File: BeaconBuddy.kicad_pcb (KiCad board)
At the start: 2 copper layers, 25.4 x 27.9 mm, 109 parts, among them P1 CONN_01X06, P2 AIN0, U1 nRF52832-QFAA, U2 Si7020-A20, U3 BMP280, Y1 32.768kHz, Y2 32MHz

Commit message: Updated Silk
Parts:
- added REF***: OSHW-Symbol_6.7x6mm_SilkScreen, Symbols:OSHW-Symbol_6.7x6mm_SilkScreen, B.Cu at (172.7, 105.9)
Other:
- board text removed: "Rypple.io"

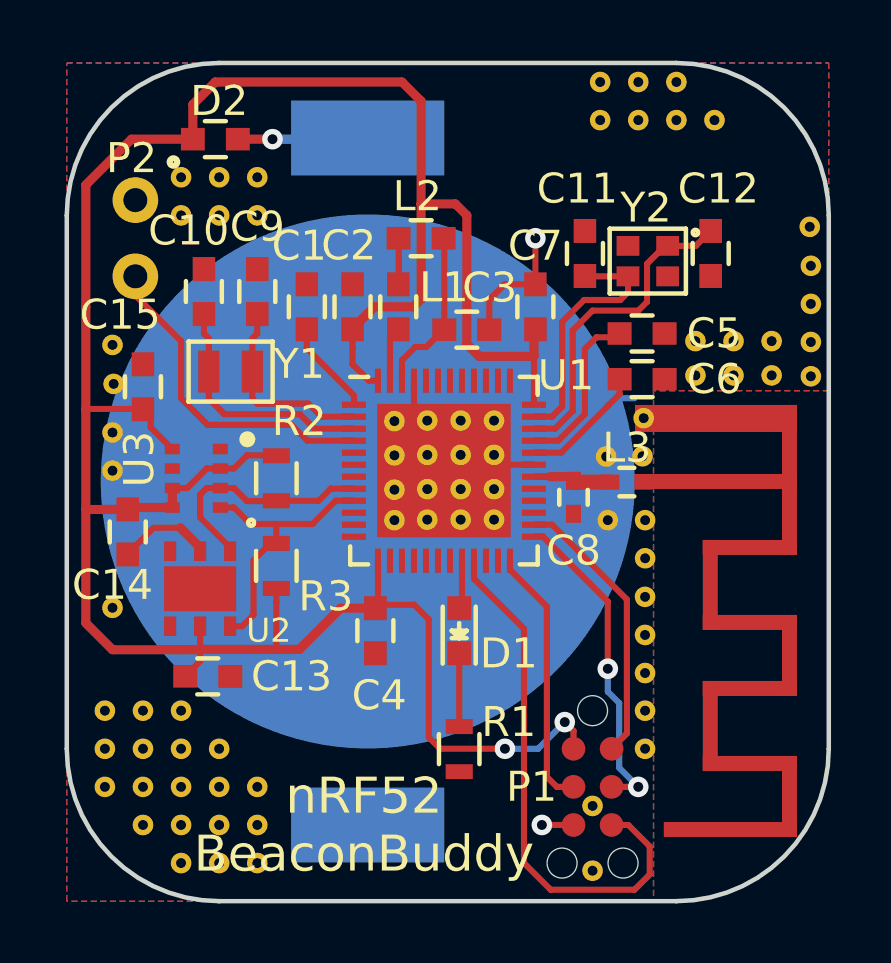
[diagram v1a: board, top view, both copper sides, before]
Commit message: Switch to BME280, update PCB
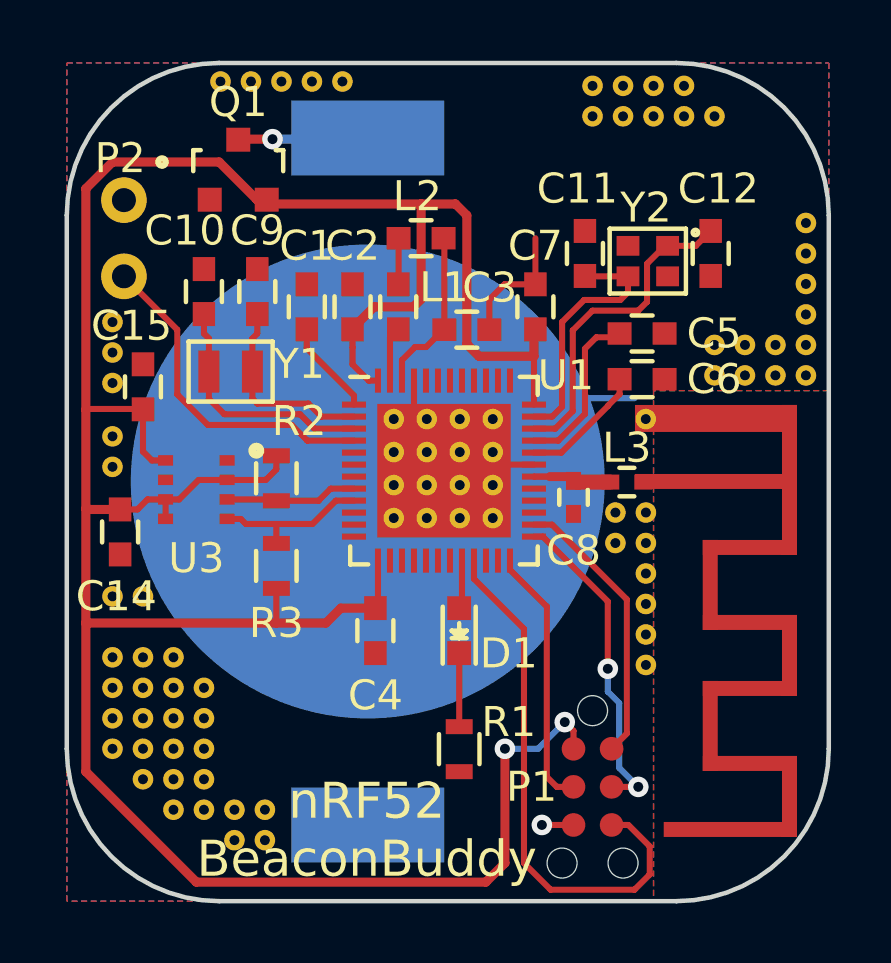
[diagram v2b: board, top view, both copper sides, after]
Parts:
- removed C13: 0.1uF, Capacitors_SMD:C_0603
- removed D2: CDBU0240, Capacitors_SMD:C_0603
- removed the REF** at (171.7, 123.2)
- removed the REF** at (171.6, 112.2)
- removed the REF** at (163.3, 115.6)
- removed the REF** at (164.4, 115.6)
- removed the REF** at (166.6, 115.6)
- removed the REF** at (165.5, 115.6)
- removed the REF** at (163.3, 114.6)
- removed the REF** at (164.4, 114.5)
- removed the REF** at (166.6, 114.5)
- removed the REF** at (165.5, 114.5)
- removed the REF** at (163.3, 113.4)
- removed the REF** at (171.7, 121.9)
- removed the REF** at (164.4, 113.4)
- removed the REF** at (166.6, 113.4)
- removed the REF** at (165.5, 113.4)
- removed the REF** at (166.6, 112.3)
- removed the REF** at (165.5, 112.3)
- removed the REF** at (164.4, 112.3)
- removed the REF** at (163.3, 112.3)
- removed the REF** at (169.9, 127.3)
- removed the REF** at (169.9, 125.1)
- removed the REF** at (153.9, 118.5)
- removed the REF** at (170.4, 115.6)
- removed the REF** at (153.9, 109.7)
- removed the REF** at (153.9, 113.9)
- removed the REF** at (153.9, 112.6)
- removed the REF** at (154.0, 111.0)
- removed the REF** at (171.7, 115.6)
- removed the REF** at (171.7, 116.8)
- removed the REF** at (177.2, 107.1)
- removed the REF** at (177.2, 108.4)
- removed the REF** at (177.2, 109.6)
- removed the REF** at (171.7, 118.1)
- removed the REF** at (177.2, 110.8)
- removed the REF** at (171.7, 119.4)
- removed the REF** at (171.7, 120.7)
- removed the REF** at (175.9, 109.6)
- removed the REF** at (174.6, 109.6)
- removed the REF** at (173.4, 109.6)
- removed the REF** at (177.2, 105.8)
- removed the REF** at (175.9, 110.7)
- removed the REF** at (173.4, 110.7)
- removed the REF** at (174.6, 110.7)
- removed the REF** at (170.4, 113.5)
- removed the REF** at (171.6, 113.4)
- removed REF***: OSHW-Symbol_6.7x6mm_SilkScreen, Symbols:OSHW-Symbol_6.7x6mm_SilkScreen
- removed REF**11, REF**12, REF**21 (x4), REF**22 (x2), REF**31 (x5), REF**32 (x4), REF**41 (x4), REF**42 (x4), REF**51 (x2), REF**52 (x5): Via-13mil, New_Footprints:Via-13mil
- removed U2: Si7020-A20, New_Footprints:S-PWSON-N6
- added Q1: Si2365EDS, TO_SOT_Packages_SMD:SOT-23, F.Cu at (158.1, 103.9)
- added REF**: Via-13mil, new_footprints:Via-13mil, F.Cu at (158.5, 100.9)
- added REF**: Via-13mil, new_footprints:Via-13mil, F.Cu at (166.6, 112.2)
- added REF**: Via-13mil, new_footprints:Via-13mil, F.Cu at (165.5, 112.2)
- added REF**: Via-13mil, new_footprints:Via-13mil, F.Cu at (165.5, 113.3)
- added REF**: Via-13mil, new_footprints:Via-13mil, F.Cu at (166.6, 113.3)
- added REF**: Via-13mil, new_footprints:Via-13mil, F.Cu at (166.6, 114.4)
- added REF**: Via-13mil, new_footprints:Via-13mil, F.Cu at (165.5, 114.4)
- added REF**: Via-13mil, new_footprints:Via-13mil, F.Cu at (165.5, 115.5)
- added REF**: Via-13mil, new_footprints:Via-13mil, F.Cu at (166.6, 115.5)
- added REF**: Via-13mil, new_footprints:Via-13mil, F.Cu at (164.4, 115.5)
- added REF**: Via-13mil, new_footprints:Via-13mil, F.Cu at (164.4, 114.4)
- added REF**: Via-13mil, new_footprints:Via-13mil, F.Cu at (157.5, 100.9)
- added REF**: Via-13mil, new_footprints:Via-13mil, F.Cu at (163.3, 114.4)
- added REF**: Via-13mil, new_footprints:Via-13mil, F.Cu at (163.3, 115.5)
- added REF**: Via-13mil, new_footprints:Via-13mil, F.Cu at (154.9, 118.1)
- added REF**: Via-13mil, new_footprints:Via-13mil, F.Cu at (153.9, 118.1)
- added REF**: Via-13mil, new_footprints:Via-13mil, F.Cu at (153.9, 113.8)
- added REF**: Via-13mil, new_footprints:Via-13mil, F.Cu at (153.9, 112.8)
- added REF**: Via-13mil, new_footprints:Via-13mil, F.Cu at (153.9, 109.0)
- added REF**: Via-13mil, new_footprints:Via-13mil, F.Cu at (153.9, 110.0)
- added REF**: Via-13mil, new_footprints:Via-13mil, F.Cu at (153.9, 111.0)
- added REF**: Via-13mil, new_footprints:Via-13mil, F.Cu at (159.0, 126.2)
- added REF**: Via-13mil, new_footprints:Via-13mil, F.Cu at (161.6, 100.9)
- added REF**: Via-13mil, new_footprints:Via-13mil, F.Cu at (159.0, 125.2)
- added REF**: Via-13mil, new_footprints:Via-13mil, F.Cu at (158.0, 125.2)
- added REF**: Via-13mil, new_footprints:Via-13mil, F.Cu at (158.0, 126.2)
- added REF**: Via-13mil, new_footprints:Via-13mil, F.Cu at (157.0, 124.2)
- added REF**: Via-13mil, new_footprints:Via-13mil, F.Cu at (157.0, 125.2)
- added REF**: Via-13mil, new_footprints:Via-13mil, F.Cu at (157.0, 123.2)
- added REF**: Via-13mil, new_footprints:Via-13mil, F.Cu at (157.0, 122.2)
- added REF**: Via-13mil, new_footprints:Via-13mil, F.Cu at (157.0, 121.2)
- added REF**: Via-13mil, new_footprints:Via-13mil, F.Cu at (156.0, 124.2)
- added REF**: Via-13mil, new_footprints:Via-13mil, F.Cu at (156.0, 123.2)
- added REF**: Via-13mil, new_footprints:Via-13mil, F.Cu at (160.6, 100.9)
- added REF**: Via-13mil, new_footprints:Via-13mil, F.Cu at (156.0, 125.2)
- added REF**: Via-13mil, new_footprints:Via-13mil, F.Cu at (156.0, 122.2)
- added REF**: Via-13mil, new_footprints:Via-13mil, F.Cu at (156.0, 121.2)
- added REF**: Via-13mil, new_footprints:Via-13mil, F.Cu at (156.0, 120.1)
- added REF**: Via-13mil, new_footprints:Via-13mil, F.Cu at (154.9, 124.2)
- added REF**: Via-13mil, new_footprints:Via-13mil, F.Cu at (154.9, 122.2)
- added REF**: Via-13mil, new_footprints:Via-13mil, F.Cu at (154.9, 123.2)
- added REF**: Via-13mil, new_footprints:Via-13mil, F.Cu at (154.9, 120.1)
- added REF**: Via-13mil, new_footprints:Via-13mil, F.Cu at (154.9, 121.2)
- added REF**: Via-13mil, new_footprints:Via-13mil, F.Cu at (153.9, 122.2)
- added REF**: Via-13mil, new_footprints:Via-13mil, F.Cu at (159.6, 100.9)
- added REF**: Via-13mil, new_footprints:Via-13mil, F.Cu at (153.9, 123.2)
- added REF**: Via-13mil, new_footprints:Via-13mil, F.Cu at (153.9, 121.2)
- added REF**: Via-13mil, new_footprints:Via-13mil, F.Cu at (153.9, 120.1)
- added REF**: Via-13mil, new_footprints:Via-13mil, F.Cu at (173.0, 102.1)
- added REF**: Via-13mil, new_footprints:Via-13mil, F.Cu at (174.0, 102.1)
- added REF**: Via-13mil, new_footprints:Via-13mil, F.Cu at (173.0, 101.1)
- added REF**: Via-13mil, new_footprints:Via-13mil, F.Cu at (172.0, 102.1)
- added REF**: Via-13mil, new_footprints:Via-13mil, F.Cu at (172.0, 101.1)
- added REF**: Via-13mil, new_footprints:Via-13mil, F.Cu at (170.9, 101.1)
- added REF**: Via-13mil, new_footprints:Via-13mil, F.Cu at (170.9, 102.1)
- added REF**: Via-13mil, new_footprints:Via-13mil, F.Cu at (164.4, 112.2)
- added REF**: Via-13mil, new_footprints:Via-13mil, F.Cu at (169.9, 101.1)
- added REF**: Via-13mil, new_footprints:Via-13mil, F.Cu at (169.9, 102.1)
- added REF**: Via-13mil, new_footprints:Via-13mil, F.Cu at (170.7, 116.3)
- added REF**: Via-13mil, new_footprints:Via-13mil, F.Cu at (170.7, 115.3)
- added REF**: Via-13mil, new_footprints:Via-13mil, F.Cu at (171.7, 119.4)
- added REF**: Via-13mil, new_footprints:Via-13mil, F.Cu at (171.7, 120.4)
- added REF**: Via-13mil, new_footprints:Via-13mil, F.Cu at (171.7, 118.4)
- added REF**: Via-13mil, new_footprints:Via-13mil, F.Cu at (171.7, 117.3)
- added REF**: Via-13mil, new_footprints:Via-13mil, F.Cu at (171.7, 116.3)
- added REF**: Via-13mil, new_footprints:Via-13mil, F.Cu at (171.7, 115.3)
- added REF**: Via-13mil, new_footprints:Via-13mil, F.Cu at (163.3, 112.2)
- added REF**: Via-13mil, new_footprints:Via-13mil, F.Cu at (176.0, 109.7)
- added REF**: Via-13mil, new_footprints:Via-13mil, F.Cu at (175.0, 109.7)
- added REF**: Via-13mil, new_footprints:Via-13mil, F.Cu at (174.0, 109.7)
- added REF**: Via-13mil, new_footprints:Via-13mil, F.Cu at (174.0, 110.7)
- added REF**: Via-13mil, new_footprints:Via-13mil, F.Cu at (175.0, 110.7)
- added REF**: Via-13mil, new_footprints:Via-13mil, F.Cu at (176.0, 110.7)
- added REF**: Via-13mil, new_footprints:Via-13mil, F.Cu at (177.0, 108.7)
- added REF**: Via-13mil, new_footprints:Via-13mil, F.Cu at (177.0, 110.7)
- added REF**: Via-13mil, new_footprints:Via-13mil, F.Cu at (177.0, 109.7)
- added REF**: Via-13mil, new_footprints:Via-13mil, F.Cu at (177.0, 105.7)
- added REF**: Via-13mil, new_footprints:Via-13mil, F.Cu at (163.3, 113.3)
- added REF**: Via-13mil, new_footprints:Via-13mil, F.Cu at (177.0, 106.7)
- added REF**: Via-13mil, new_footprints:Via-13mil, F.Cu at (177.0, 107.7)
- added REF**: Via-13mil, new_footprints:Via-13mil, F.Cu at (171.7, 112.2)
- added REF**: Via-13mil, new_footprints:Via-13mil, F.Cu at (164.4, 113.3)
- U3: value BMP280 -> BME280; footprint New_Footprints:Bosch_LGA8 -> new_footprints:Bosch_LGA8_2.5x2.5
- moved P2 0.38 mm to (154.3, 106.2)
- moved U3 0.38 mm to (156.7, 114.6)
- moved C14 0.25 mm to (154.2, 116.0)
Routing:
- net VDD: track 90.6 -> 98.6 mm
- net /SCL: track 9.48 -> 5.47 mm
- net /SDA: track 8.00 -> 4.56 mm
- net GND: track 20.8 -> 17.6 mm, vias 2 -> 1

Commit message: Update PCB for rev.C
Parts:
- removed the REF** at (157.0, 124.2)
- removed the REF** at (157.0, 123.2)
- removed the REF** at (157.0, 122.2)
- removed the REF** at (157.0, 121.2)
- added B1: SKRPABE010, New_Footprints:SKRPABE010, F.Cu at (159.3, 123.1)
- added D2: L0603R, LEDs:LED_0603, F.Cu at (164.2, 121.5)
- added R4: 470, Resistors_SMD:R_0603, F.Cu at (164.2, 124.8)
- added R5: 10k, Resistors_SMD:R_0603, F.Cu at (161.0, 125.9)
- moved D1 2.31 mm to (165.9, 121.5), turned to 270 degrees
- moved R1 1.68 mm to (165.9, 124.8)
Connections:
- R1 pad 1: Net-(D1-Pad1) -> Net-(D1-Pad2)
- R1 pad 2: GND -> VDD
- U1 pad 20: Net-(D1-Pad2) -> Net-(D1-Pad1)
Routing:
- net /nRESET: track 8.74 -> 19.0 mm, vias 0 -> 2
- net VDD: track 98.6 -> 103.2 mm
- net Net-(D2-Pad1): track 0.00 -> 4.26 mm
- net Net-(D2-Pad2): track 0.00 -> 1.82 mm
- net Net-(D1-Pad1): track 2.45 -> 3.98 mm
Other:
- board text added: "reset"
- board text added: "rev.c"
